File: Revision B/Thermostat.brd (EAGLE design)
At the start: 50.8 x 50.8 mm, 27 parts

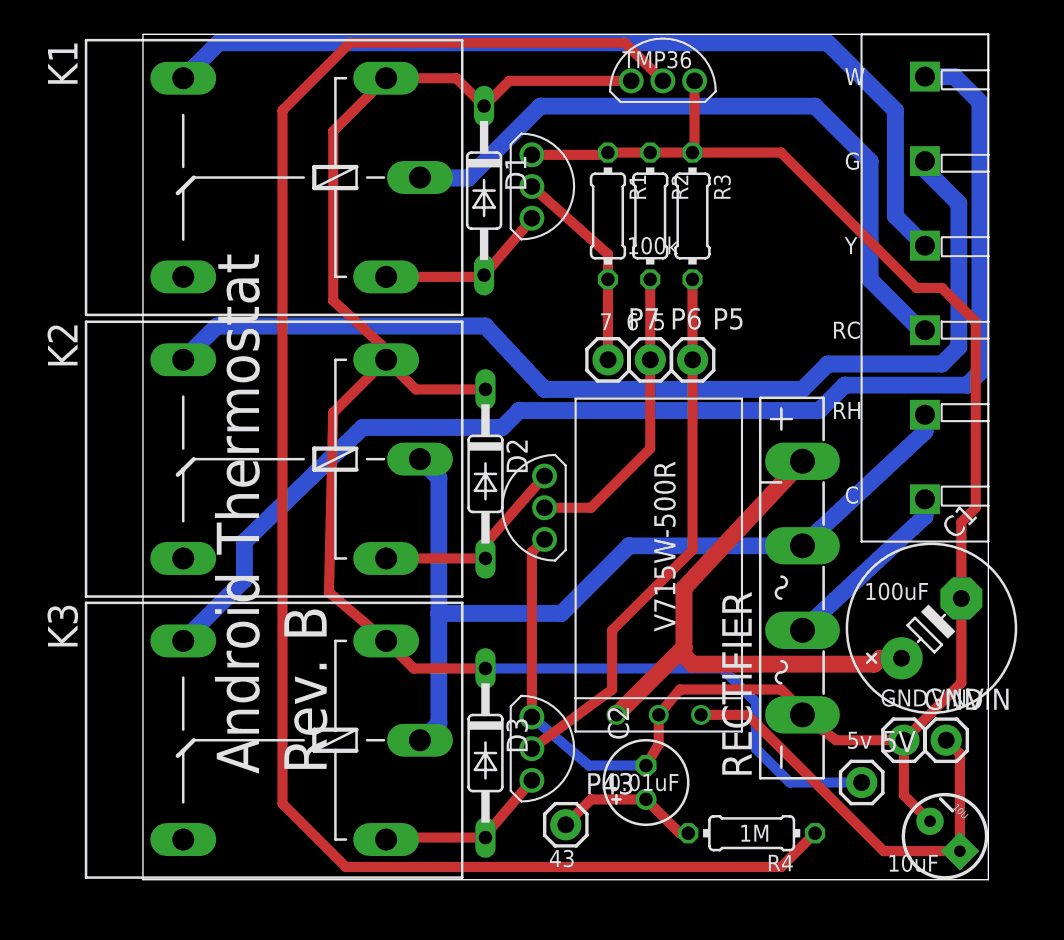
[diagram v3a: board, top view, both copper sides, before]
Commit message: Added Capacitor
Added a 0.1uF capacitor between the 5v and GND lines on the temperature
sensor to help avoid fluctuations.
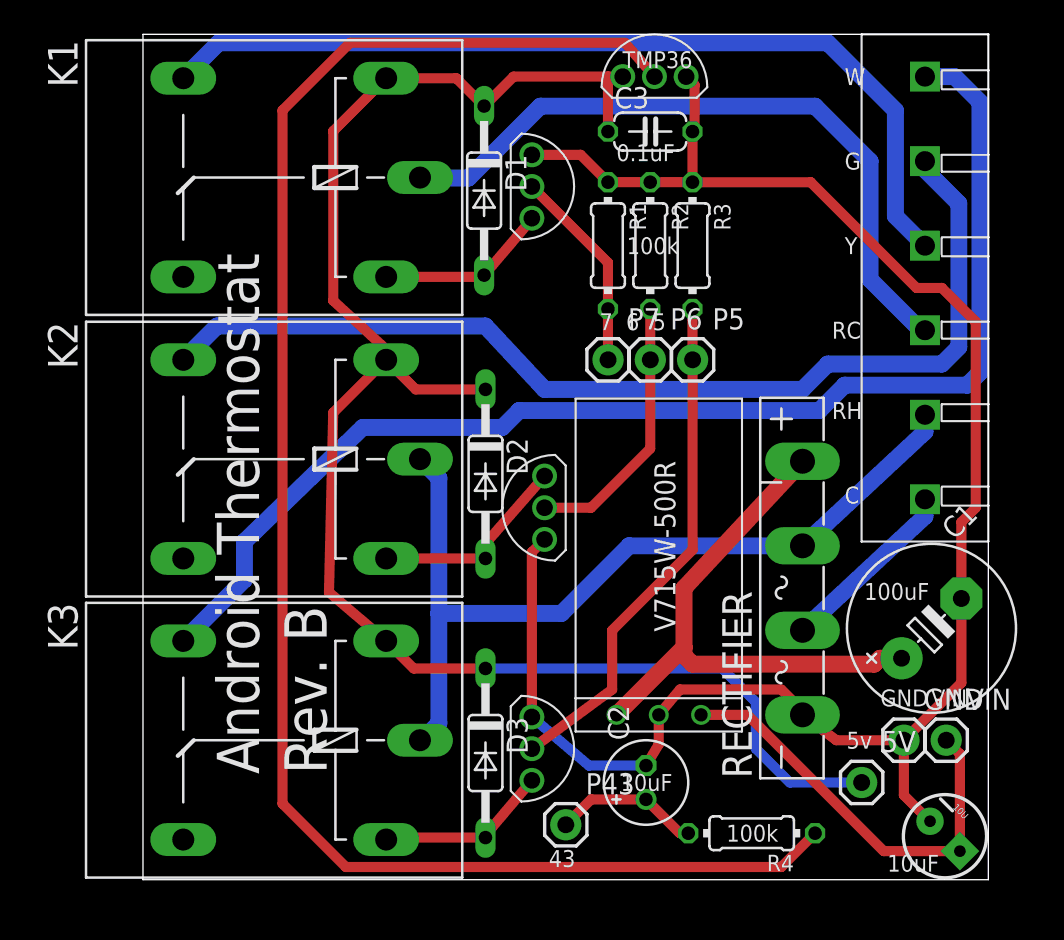
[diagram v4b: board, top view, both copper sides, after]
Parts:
- added C3: (no value), rcl:C050-024X044
- moved R1 1.78 mm to (27.9, 38.1)
- moved R2 1.78 mm to (30.5, 38.1)
- moved R3 1.78 mm to (33.0, 38.1)
- moved U$1 0.57 mm to (30.7, 48.3)
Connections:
- net +5V: now also C3.1
- net GND: now also C3.2
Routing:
- net +5V: track 95.9 -> 98.8 mm
- net GND: track 107.0 -> 109.2 mm
- net N$17: track 32.6 -> 30.9 mm
- net N$2: track 18.0 -> 16.2 mm
- net N$5: track 101.6 -> 101.0 mm
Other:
- board text added: "0.1uF"
- board text removed: "0.01uF"
- board text removed: "1M"
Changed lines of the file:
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@@
 <text x="41.402" y="27.686" size="1.016" layer="121" font="vector">RH</text>
 <text x="42.164" y="22.606" size="1.016" layer="121" font="vector">C</text>
-<text x="27.94" y="5.334" size="1.016" layer="121" font="vector">0.01uF</text>
-<text x="35.814" y="2.286" size="1.016" layer="121" font="vector">1M</text>
+<text x="35.052" y="2.286" size="1.016" layer="121" font="vector">100k</text>
+<text x="28.702" y="5.334" size="1.016" layer="121" font="vector">10uF</text>
+<text x="28.448" y="43.18" size="1.016" layer="121" font="vector">0.1uF</text>
 </plain>
 <attributes>
@@
 <element name="D2" library="diode" package="DO35-10" value="" x="20.5803" y="24.384" rot="R270"/>
 <element name="D3" library="diode" package="DO35-10" value="" x="20.5803" y="7.612" rot="R270"/>
-<element name="R1" library="rcl" package="0204/7" value="" x="27.94" y="39.8843" rot="R270"/>
-<element name="R2" library="rcl" package="0204/7" value="" x="30.48" y="39.8843" rot="R270"/>
-<element name="R3" library="rcl" package="0204/7" value="" x="33.02" y="39.8843" rot="R270"/>
+<element name="R1" library="rcl" package="0204/7" value="" x="27.94" y="38.1063" rot="R270"/>
+<element name="R2" library="rcl" package="0204/7" value="" x="30.48" y="38.1063" rot="R270"/>
+<element name="R3" library="rcl" package="0204/7" value="" x="33.02" y="38.1063" rot="R270"/>
 <element name="C2" library="rcl" package="E2-5" value="" x="30.226" y="5.842" rot="R90"/>
 <element name="U$3" library="android-thermostat" package="PHOENIX_E_5MM_6PIN" value="PHOENIX-651-1935200" x="46.99" y="35.56"/>
-<element name="U$1" library="android-thermostat" package="TMP36" value="TMP36" x="31.242" y="48.006" rot="R90"/>
+<element name="U$1" library="android-thermostat" package="TMP36" value="TMP36" x="30.734" y="48.26" rot="R90"/>
 <element name="U$4" library="android-thermostat" package="TRANSISTOR" value="TRANSISTOR" x="23.368" y="7.874"/>
 <element name="U$5" library="android-thermostat" package="TRANSISTOR" value="TRANSISTOR" x="24.13" y="22.352" rot="R180"/>
@@
 <element name="R4" library="rcl" package="0204/7" value="" x="36.576" y="2.794" rot="R180"/>
 <element name="C1" library="rcl" package="E5-10,5" value="" x="47.380028125" y="15.103975" rot="R45"/>
+<element name="C3" library="rcl" package="C050-024X044" value="" x="30.48" y="44.958"/>
 </elements>
 <signals>
@@
 <wire x1="45.7263" y1="8.382" x2="41.6623" y2="8.382" width="0.6096" layer="1"/>
 <wire x1="41.6623" y1="8.382" x2="39.6303" y2="9.906" width="0.6096" layer="1"/>
-<wire x1="33.02" y1="43.6943" x2="30.48" y2="43.6943" width="0.6096" layer="1"/>
-<wire x1="30.48" y1="43.6943" x2="27.94" y2="43.6943" width="0.6096" layer="1"/>
+<wire x1="33.02" y1="41.9163" x2="30.48" y2="41.9163" width="0.6096" layer="1"/>
+<wire x1="30.48" y1="41.9163" x2="27.94" y2="41.9163" width="0.6096" layer="1"/>
 <wire x1="50.038" y1="22.352" x2="50.038" y2="33.528" width="0.6096" layer="1"/>
 <contactref element="C1" pad="-"/>
@@
 <wire x1="49.176078125" y1="16.900025" x2="49.176078125" y2="21.490078125" width="0.6096" layer="1"/>
 <wire x1="49.176078125" y1="21.490078125" x2="50.038" y2="22.352" width="0.6096" layer="1"/>
-<wire x1="38.3477" y1="43.6943" x2="46.482" y2="35.56" width="0.6096" layer="1"/>
 <wire x1="46.482" y1="35.56" x2="48.006" y2="35.56" width="0.6096" layer="1"/>
 <wire x1="48.006" y1="35.56" x2="50.038" y2="33.528" width="0.6096" layer="1"/>
-<wire x1="23.368" y1="43.561" x2="27.8067" y2="43.561" width="0.6096" layer="1"/>
-<wire x1="27.8067" y1="43.561" x2="27.94" y2="43.6943" width="0.6096" layer="1"/>
-<wire x1="33.02" y1="43.6943" x2="38.3477" y2="43.6943" width="0.6096" layer="1"/>
 <wire x1="30.226" y1="6.858" x2="26.797" y2="6.858" width="0.6096" layer="16"/>
 <wire x1="26.797" y1="6.858" x2="23.368" y2="9.779" width="0.6096" layer="16"/>
@@
 <wire x1="30.9943" y1="9.906" x2="30.9943" y2="8.1343" width="0.6096" layer="1"/>
 <wire x1="30.9943" y1="8.1343" x2="30.226" y2="6.858" width="0.6096" layer="1"/>
-<wire x1="33.147" y1="48.006" x2="33.147" y2="43.8213" width="0.6096" layer="1"/>
-<wire x1="33.147" y1="43.8213" x2="33.02" y2="43.6943" width="0.6096" layer="1"/>
+<contactref element="C3" pad="2"/>
+<wire x1="33.02" y1="41.9163" x2="33.02" y2="44.958" width="0.6096" layer="1"/>
+<wire x1="33.02" y1="44.958" x2="33.147" y2="44.958" width="0.6096" layer="1"/>
+<wire x1="33.147" y1="44.958" x2="33.147" y2="47.752" width="0.6096" layer="1"/>
+<wire x1="33.147" y1="47.752" x2="32.639" y2="48.26" width="0.6096" layer="1"/>
+<wire x1="23.368" y1="43.561" x2="26.2953" y2="43.561" width="0.6096" layer="1"/>
+<wire x1="26.2953" y1="43.561" x2="27.94" y2="41.9163" width="0.6096" layer="1"/>
+<wire x1="46.482" y1="35.56" x2="40.132" y2="41.91" width="0.6096" layer="1"/>
+<wire x1="40.132" y1="41.91" x2="33.0263" y2="41.91" width="0.6096" layer="1"/>
+<wire x1="33.0263" y1="41.91" x2="33.02" y2="41.9163" width="0.6096" layer="1"/>
 </signal>
 <signal name="N$2">
@@
 <contactref element="P6" pad="1"/>
 <contactref element="U$5" pad="G"/>
-<wire x1="30.48" y1="36.0743" x2="30.48" y2="31.2483" width="0.6096" layer="1"/>
+<wire x1="30.48" y1="34.2963" x2="30.48" y2="31.2483" width="0.6096" layer="1"/>
 <wire x1="30.48" y1="31.2483" x2="30.4863" y2="31.242" width="0.6096" layer="1"/>
 <wire x1="24.13" y1="22.352" x2="26.924" y2="22.352" width="0.6096" layer="1"/>
@@
 <wire x1="36.83" y1="7.874" x2="38.862" y2="5.842" width="0.6096" layer="16"/>
 <wire x1="38.862" y1="5.842" x2="43.1863" y2="5.842" width="0.6096" layer="16"/>
-<wire x1="29.337" y1="48.006" x2="22.012859375" y2="48.006" width="0.6096" layer="1"/>
-<wire x1="22.012859375" y1="48.006" x2="20.496478125" y2="46.48961875" width="0.6096" layer="1"/>
+<contactref element="C3" pad="1"/>
+<wire x1="28.829" y1="48.26" x2="27.94" y2="48.26" width="0.6096" layer="1"/>
+<wire x1="27.94" y1="48.26" x2="22.266859375" y2="48.26" width="0.6096" layer="1"/>
+<wire x1="22.266859375" y1="48.26" x2="20.496478125" y2="46.48961875" width="0.6096" layer="1"/>
+<wire x1="27.94" y1="44.958" x2="27.94" y2="48.26" width="0.6096" layer="1"/>
 </signal>
 <signal name="N$3">
@@
 <contactref element="R1" pad="2"/>
 <contactref element="U$6" pad="G"/>
-<wire x1="27.94" y1="36.0743" x2="27.94" y2="31.2483" width="0.6096" layer="1"/>
+<wire x1="27.94" y1="34.2963" x2="27.94" y2="31.2483" width="0.6096" layer="1"/>
 <wire x1="27.94" y1="31.2483" x2="27.9463" y2="31.242" width="0.6096" layer="1"/>
-<wire x1="27.94" y1="36.0743" x2="27.94" y2="37.592" width="0.6096" layer="1"/>
-<wire x1="27.94" y1="37.592" x2="23.368" y2="41.656" width="0.6096" layer="1"/>
+<wire x1="27.94" y1="34.2963" x2="27.94" y2="37.084" width="0.6096" layer="1"/>
+<wire x1="27.94" y1="37.084" x2="23.368" y2="41.656" width="0.6096" layer="1"/>
 </signal>
 <signal name="N$7">
@@
 <contactref element="R3" pad="2"/>
 <contactref element="U$4" pad="G"/>
-<wire x1="33.02" y1="36.0743" x2="33.02" y2="31.2483" width="0.6096" layer="1"/>
+<wire x1="33.02" y1="34.2963" x2="33.02" y2="31.2483" width="0.6096" layer="1"/>
 <wire x1="33.02" y1="31.2483" x2="33.0263" y2="31.242" width="0.6096" layer="1"/>
 <wire x1="33.0263" y1="31.242" x2="33.0263" y2="19.8183" width="0.6096" layer="1"/>
@@
 <contactref element="U$1" pad="OUT2"/>
 <contactref element="R4" pad="1"/>
-<wire x1="31.242" y1="48.006" x2="28.956" y2="50.292" width="0.6096" layer="1"/>
+<wire x1="30.734" y1="48.26" x2="28.956" y2="50.292" width="0.6096" layer="1"/>
 <wire x1="28.956" y1="50.292" x2="12.446" y2="50.292" width="0.6096" layer="1"/>
 <wire x1="12.446" y1="50.292" x2="8.382" y2="46.228" width="0.6096" layer="1"/>
